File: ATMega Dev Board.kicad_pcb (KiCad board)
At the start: 4 copper layers, 88 x 43 mm, 58 parts, among them J1 Conn_01x13, J2 Conn_01x09, J3 SPI header, J4 USB-C_31-M-12, Q1 S8050, Q2 2N7002, Q3 HL6042, Q4 HL6042, SW1 SW_SPST, SW2 SW_SPST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

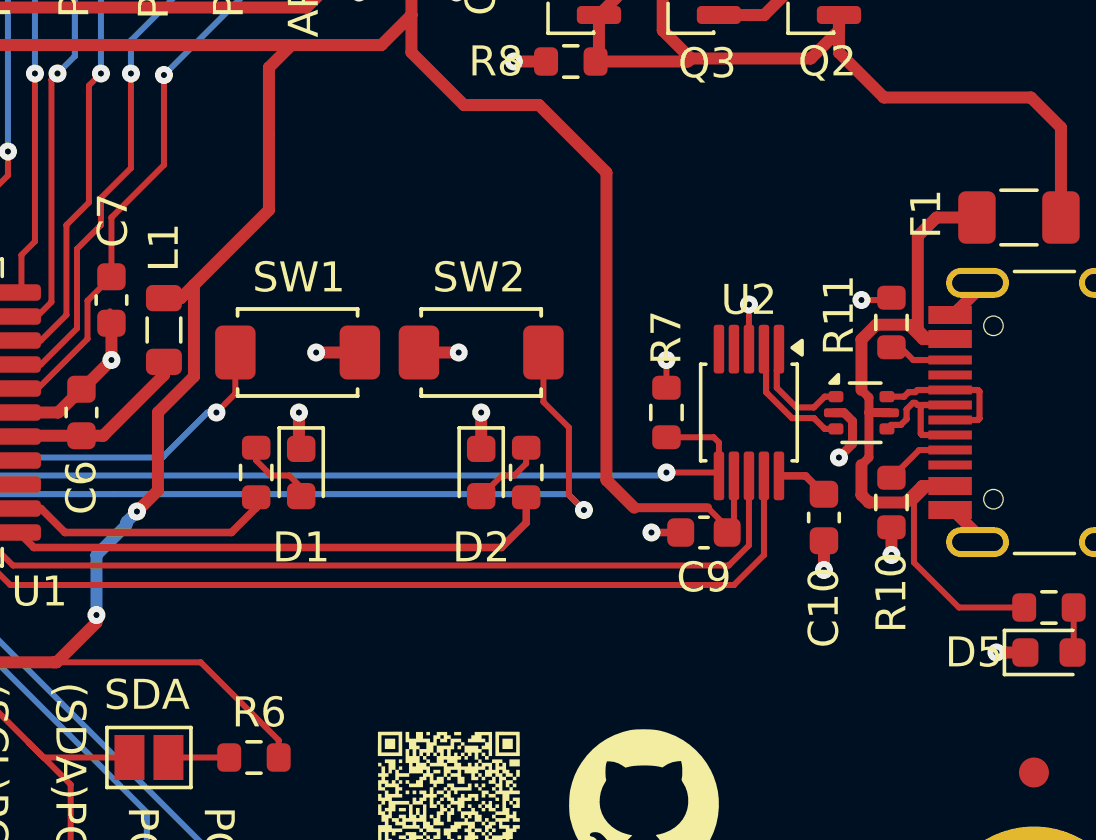
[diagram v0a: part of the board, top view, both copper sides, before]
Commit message: added VBUS capacitor
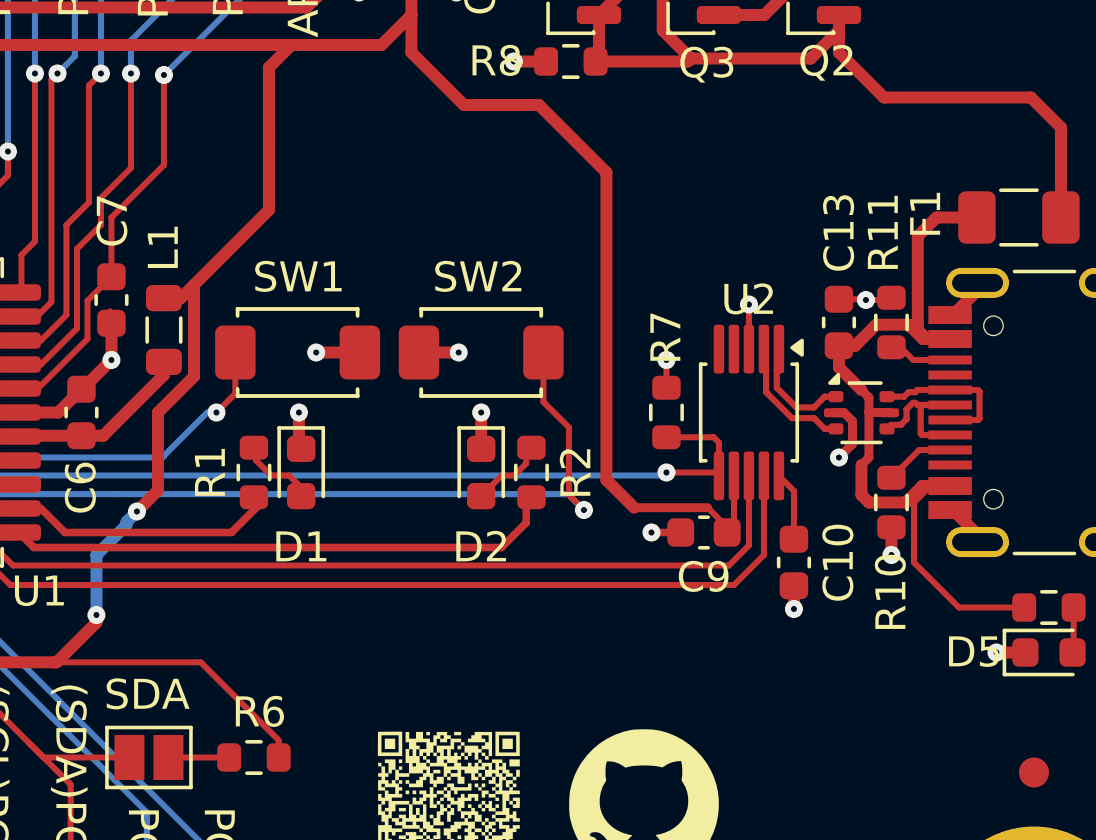
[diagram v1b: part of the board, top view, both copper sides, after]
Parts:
- added C13: 0.1u, Capacitor_SMD:C_0603_1608Metric, F.Cu at (115.1, 62.4)
- J1: value Conn_01x13 -> Conn_01x14
- J2: value Conn_01x09 -> Conn_01x11
- R1, R2: value 220 -> 510
- moved C10 1.80 mm to (113.6, 70.4)
- moved R2 0.17 mm to (104.8, 67.4)
- moved R1 0.08 mm to (95.6, 67.4)
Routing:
- net VBUS: track 27.0 -> 27.9 mm
- net GND: track 39.3 -> 40.1 mm

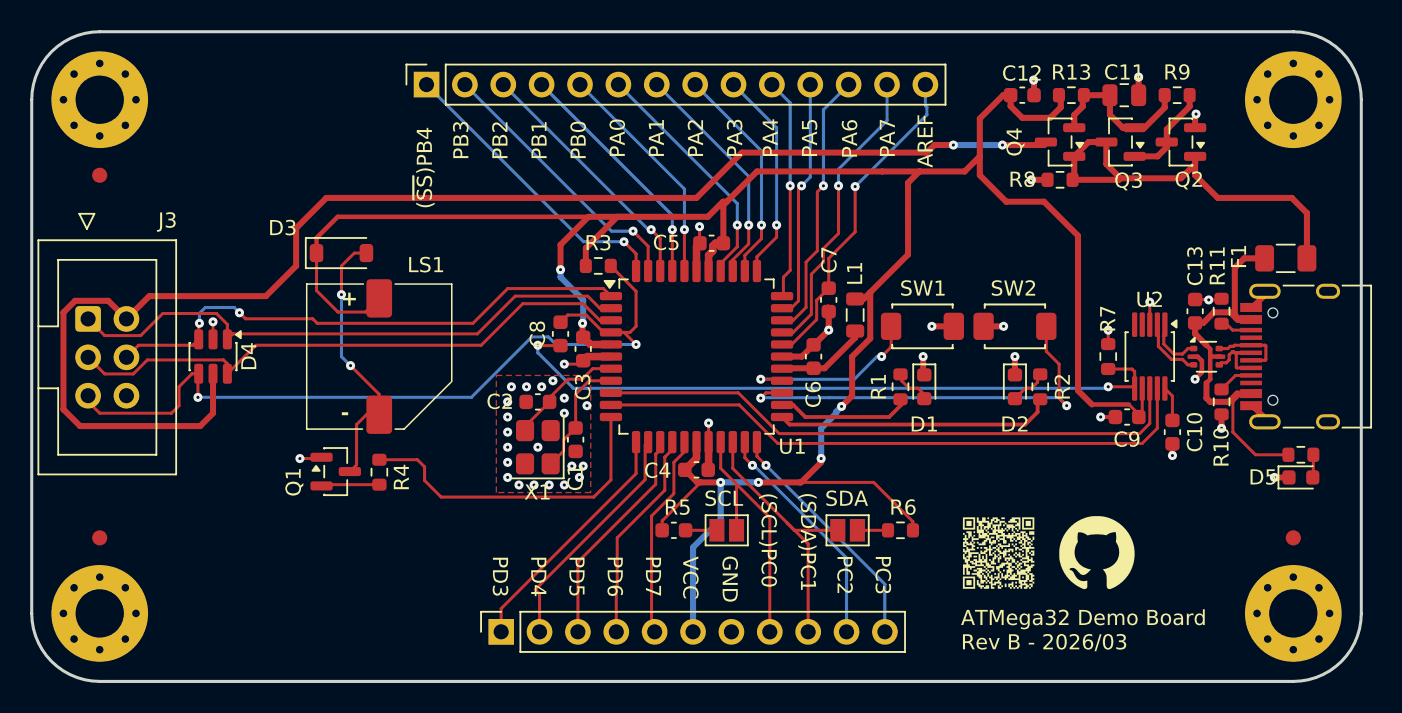
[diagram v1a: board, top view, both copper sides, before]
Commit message: fixed CH340X DTR setup
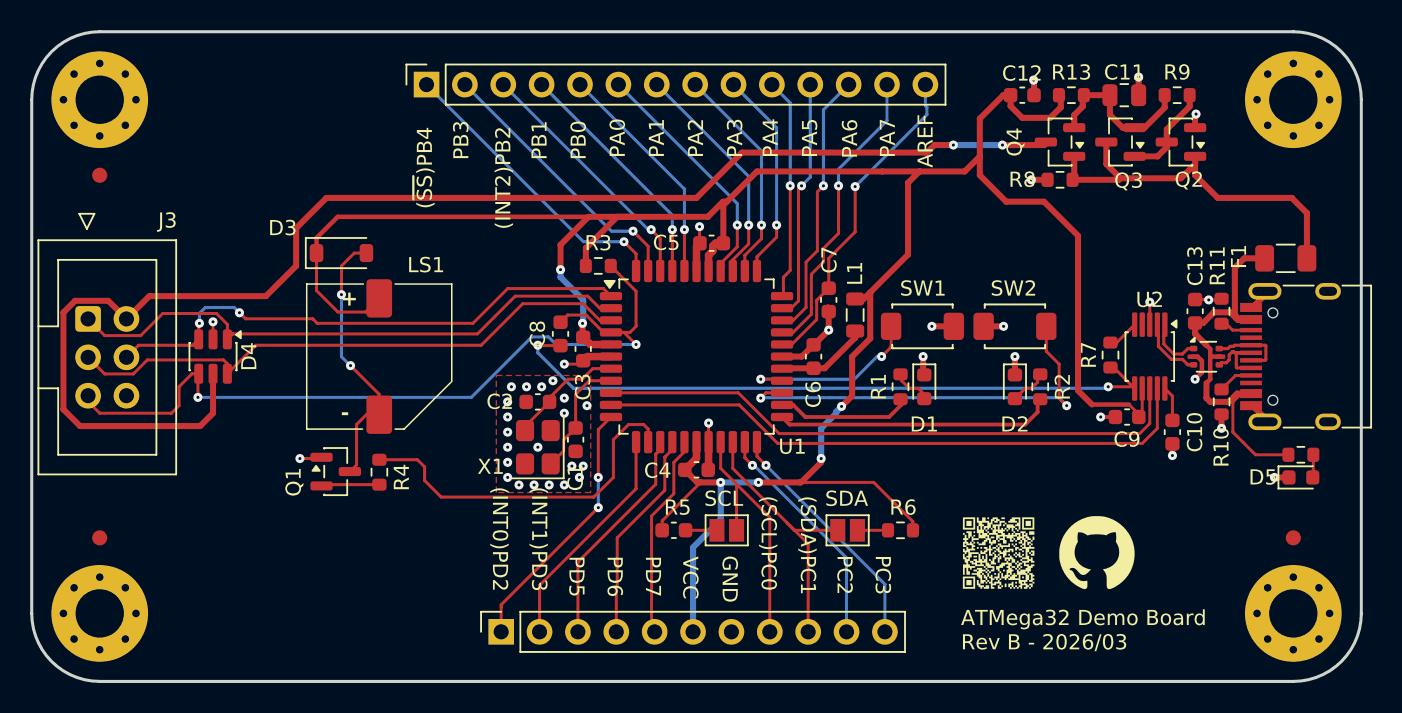
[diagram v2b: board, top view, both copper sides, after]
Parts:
- moved R7 0.18 mm to (109.5, 65.3)
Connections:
- J2 pad 1: /PD3 -> /PD2
- J2 pad 2: /PD4 -> /PD3
- R7 pad 2: GND -> Net-(U2-~{CTS})
- U1 pad 11: /SPKR -> /PD2
- U1 pad 13: /PD4 -> /SPKR
- U2 pad 5: unconnected-(U2-~{CTS}-Pad5) -> Net-(U2-~{CTS})
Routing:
- net /PD2: track 0.00 -> 17.2 mm, vias 0 -> 2
- net /PD4: track 15.8 -> 0.00 mm
- net VUSB: track 28.6 -> 26.1 mm
- net /SPKR: track 21.5 -> 23.8 mm
- net Net-(U2-~{CTS}): track 0.00 -> 2.09 mm
- net /PD3: track 16.3 -> 15.2 mm
- net GND: track 40.1 -> 39.2 mm, vias 43 -> 42
- net /DTR: track 45.5 -> 44.7 mm
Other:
- board text added: "(INT0)PD2"
- board text added: "(INT1)PD3"
- board text added: "(INT2)PB2"
- board text removed: "PB2"
- board text removed: "PD3"
- board text removed: "PD4"
